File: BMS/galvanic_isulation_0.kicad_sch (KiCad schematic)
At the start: 12 parts

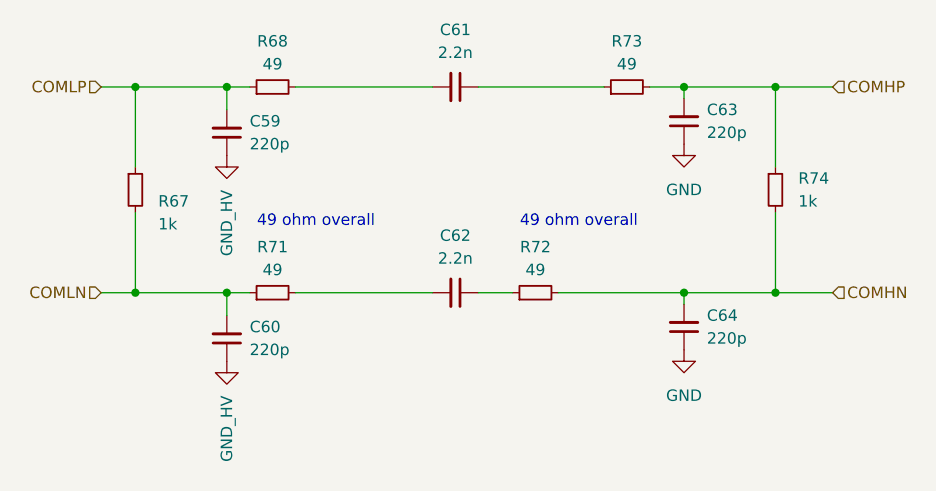
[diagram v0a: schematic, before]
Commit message: Dodano layout drugiego bq79614, ukladu tlumaczącego z protokułu TI na UART oraz wstępnie poprowadzono pary różnicowe
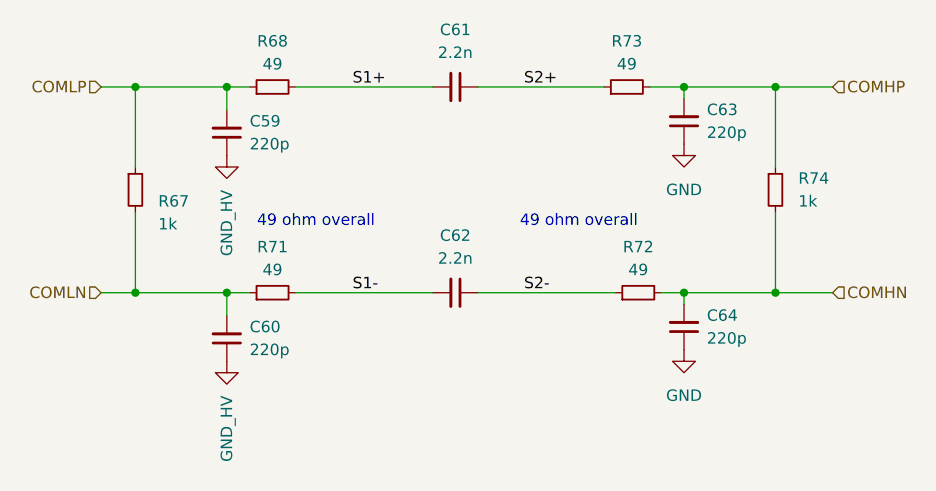
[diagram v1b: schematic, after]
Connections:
- net S1+: now reaches C61.2, R68.2
- net S2+: now reaches C61.1, R73.1
- net S2-: now reaches C62.1, R72.1
- net S1-: now reaches C62.2, R71.2
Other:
- moved on the sheet: R72
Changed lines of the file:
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@@
 	(wire
 		(pts
-			(xy 130.81 97.79) (xy 144.78 97.79)
+			(xy 142.24 97.79) (xy 144.78 97.79)
 		)
 		(stroke
@@
 	(wire
 		(pts
-			(xy 125.73 97.79) (xy 121.92 97.79)
+			(xy 137.16 97.79) (xy 121.92 97.79)
 		)
 		(stroke
@@
 		)
 	)
+	(label "S2+"
+		(at 127 74.93 0)
+		(fields_autoplaced yes)
+		(effects
+			(font
+				(size 1.27 1.27)
+			)
+			(justify left bottom)
+		)
+	)
+	(label "S2-"
+		(at 127 97.79 0)
+		(fields_autoplaced yes)
+		(effects
+			(font
+				(size 1.27 1.27)
+			)
+			(justify left bottom)
+		)
+	)
+	(label "S1-"
+		(at 107.95 97.79 0)
+		(fields_autoplaced yes)
+		(effects
+			(font
+				(size 1.27 1.27)
+			)
+			(justify left bottom)
+		)
+	)
+	(label "S1+"
+		(at 107.95 74.93 0)
+		(fields_autoplaced yes)
+		(effects
+			(font
+				(size 1.27 1.27)
+			)
+			(justify left bottom)
+		)
+	)
 	(hierarchical_label "COMLP"
 		(shape input)
@@
 	(symbol
 		(lib_id "Device:R_Small")
-		(at 128.27 97.79 90)
+		(at 139.7 97.79 90)
 		(unit 1)
 		(exclude_from_sim no)
@@
 		(fields_autoplaced yes)
 		(property "Reference" "R72"
-			(at 128.27 92.71 90)
+			(at 139.7 92.71 90)
 			(effects
 				(font
@@
 		)
 		(property "Value" "49"
-			(at 128.27 95.25 90)
+			(at 139.7 95.25 90)
 			(effects
 				(font
@@
 		)
 		(property "Footprint" "Resistor_SMD:R_0603_1608Metric_Pad0.98x0.95mm_HandSolder"
-			(at 128.27 97.79 0)
+			(at 139.7 97.79 0)
 			(effects
 				(font
@@
 		)
 		(property "Datasheet" "https://www.mouser.pl/ProductDetail/KOA-Speer/RK73H1HRTTCM49R9F?qs=sGAEpiMZZMvdGkrng054txLI%2FDB4oIKDjd1z9Y%252BmyaXFChdzxTCbsQ%3D%3D"
-			(at 128.27 97.79 0)
+			(at 139.7 97.79 0)
 			(effects
 				(font
@@
 		)
 		(property "Description" "Resistor, small symbol"
-			(at 128.27 97.79 0)
-			(effects
-				(font
+			(at 139.7 97.79 0)
+			(effects
+				(font

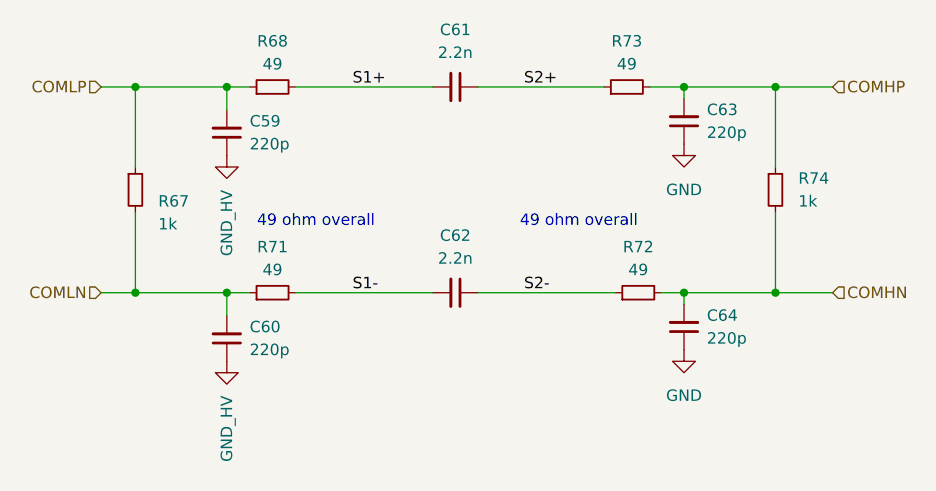
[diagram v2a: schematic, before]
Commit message: Zmienione kondensatory na kondensatory bezpieczeństwa,poprawiono strefy na thermal relief oraz naprawiono bledy z tym zwiazane, impedancja do zmiany jeszcze
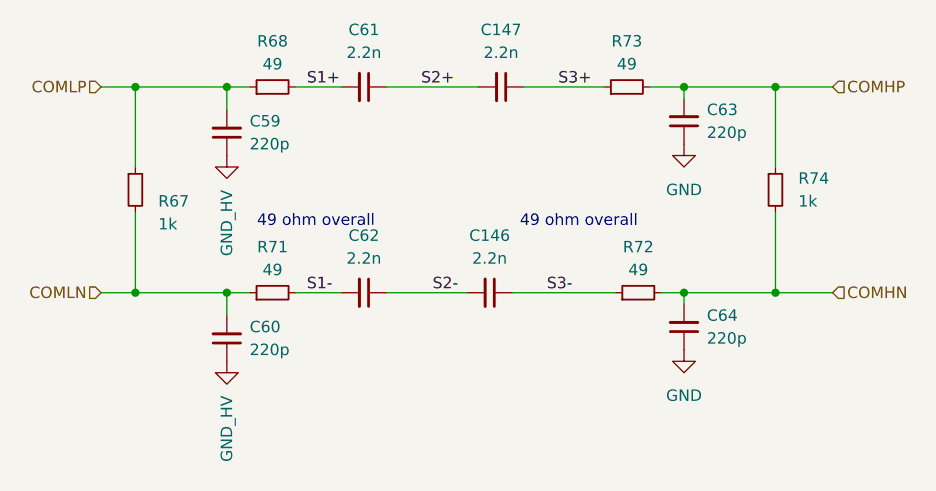
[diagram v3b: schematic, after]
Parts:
- added C146, C147: 2.2n, footrpint:CAPC5728X280N, symbol Device:C_Small
- C61, C62: footprint Capacitor_SMD:C_0603_1608Metric_Pad1.08x0.95mm_HandSolder -> footrpint:CAPC5728X280N
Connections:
- net S2+: now also C147.2; no longer R73.1
- net S2-: now also C146.2; no longer R72.1
- new net S3+: C147.1, R73.1
- new net S3-: C146.1, R72.1
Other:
- moved on the sheet: C61, C62
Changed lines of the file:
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@@
-	(wire
-		(pts
-			(xy 121.92 74.93) (xy 135.89 74.93)
-		)
-		(stroke
-			(width 0)
-			(type default)
-		)
-	)
 	(wire
 		(pts
@@
 	(wire
 		(pts
-			(xy 101.6 97.79) (xy 116.84 97.79)
+			(xy 111.76 97.79) (xy 120.65 97.79)
+		)
+		(stroke
+			(width 0)
+			(type default)
+		)
+	)
+	(wire
+		(pts
+			(xy 101.6 97.79) (xy 106.68 97.79)
 		)
 		(stroke
@@
 	(wire
 		(pts
-			(xy 101.6 74.93) (xy 116.84 74.93)
+			(xy 101.6 74.93) (xy 106.68 74.93)
 		)
 		(stroke
@@
 	(wire
 		(pts
+			(xy 125.73 97.79) (xy 137.16 97.79)
+		)
+		(stroke
+			(width 0)
+			(type default)
+		)
+	)
+	(wire
+		(pts
 			(xy 83.82 88.9) (xy 83.82 97.79)
 		)
@@
 	(wire
 		(pts
+			(xy 111.76 74.93) (xy 121.92 74.93)
+		)
+		(stroke
+			(width 0)
+			(type default)
+		)
+	)
+	(wire
+		(pts
 			(xy 144.78 97.79) (xy 154.94 97.79)
 		)
@@
 	(wire
 		(pts
-			(xy 137.16 97.79) (xy 121.92 97.79)
+			(xy 127 74.93) (xy 135.89 74.93)
 		)
 		(stroke
@@
 	)
 	(label "S2+"
-		(at 127 74.93 0)
+		(at 115.57 74.93 0)
 		(effects
 			(font
@@
 		)
 	)
-	(label "S2-"
-		(at 127 97.79 0)
+	(label "S3+"
+		(at 130.81 74.93 0)
 		(effects
 			(font
@@
 		)
 	)
-	(label "S1-"
-		(at 107.95 97.79 0)
+	(label "S2-"
+		(at 116.84 97.79 0)
 		(effects
 			(font
@@
 		)
 	)
+	(label "S1-"
+		(at 102.87 97.79 0)
+		(effects
+			(font
+				(size 1.27 1.27)
+			)
+			(justify left bottom)
+		)
+	)
+	(label "S3-"
+		(at 129.54 97.79 0)
+		(effects
+			(font
+				(size 1.27 1.27)
+			)
+			(justify left bottom)
+		)
+	)
 	(label "S1+"
-		(at 107.95 74.93 0)
+		(at 102.87 74.93 0)
 		(effects
 			(font
@@
 	(symbol
 		(lib_id "Device:C_Small")
-		(at 119.38 74.93 270)
+		(at 109.22 74.93 270)
 		(unit 1)
 		(exclude_from_sim no)
@@
 		(fields_autoplaced yes)
 		(property "Reference" "C61"
-			(at 119.3736 68.58 90)
+			(at 109.2136 68.58 90)
 			(effects
 				(font
@@
 		)
 		(property "Value" "2.2n"
-			(at 119.3736 71.12 90)
-			(effects
-				(font
-					(size 1.27 1.27)
-				)
-			)
-		)
-		(property "Footprint" "Capacitor_SMD:C_0603_1608Metric_Pad1.08x0.95mm_HandSolder"
-			(at 119.38 74.93 0)
-			(effects
-				(font
-					(size 1.27 1.27)
-				)
-				(hide yes)
-			)
-		)
-		(property "Datasheet" "https://www.mouser.pl/ProductDetail/TDK/CGA3E2C0G1H222J080AE?qs=P1JMDcb91o5KNu2GzASXrQ%3D%3D"
-			(at 119.38 74.93 0)
-			(effects
-				(font
-					(size 1.27 1.27)
-				)
-				(hide yes)
-			)
-		)
-		(property "Description" "Unpolarized capacitor, small symbol"
-			(at 119.38 74.93 0)
+			(at 109.2136 71.12 90)
+			(effects
+				(font
+					(size 1.27 1.27)
+				)
+			)
+		)
+		(property "Footprint" "footrpint:CAPC5728X280N"
+			(at 109.22 74.93 0)
+			(effects
+				(font
+					(size 1.27 1.27)
+				)
+				(hide yes)
+			)
+		)
+		(property "Datasheet" "https://www.mouser.pl/ProductDetail/Walsin/S252B222K502CT?qs=wUXugUrL1qx2Bha0j7hz5g%3D%3D"
+			(at 109.22 74.93 0)
+			(effects
+				(font
+					(size 1.27 1.27)
+				)
+				(hide yes)
+			)
+		)
+		(property "Description" "Kondensator Bezpieczeństwa 250V"
+			(at 109.22 74.93 0)
 			(effects
 				(font
@@
 				(path "/26289bb6-56bc-4ca1-b1a2-18d58d1afdf5/40b62235-494b-489c-87ee-38a07fa46b52"
 					(reference "C61")
+					(unit 1)
+				)
+			)
+		)
+	)
+	(symbol
+		(lib_id "Device:C_Small")
+		(at 123.19 97.79 270)
+		(unit 1)
+		(exclude_from_sim no)
+		(in_bom yes)
+		(on_board yes)
+		(dnp no)
+		(fields_autoplaced yes)
+		(property "Reference" "C146"
+			(at 123.1836 91.44 90)
+			(effects
+				(font
+					(size 1.27 1.27)
+				)
+			)
+		)
+		(property "Value" "2.2n"
+			(at 123.1836 93.98 90)
+			(effects
+				(font
+					(size 1.27 1.27)
+				)
+			)
+		)
+		(property "Footprint" "footrpint:CAPC5728X280N"
+			(at 123.19 97.79 0)
+			(effects
+				(font
+					(size 1.27 1.27)
+				)
+				(hide yes)
+			)
+		)
+		(property "Datasheet" "https://www.mouser.pl/ProductDetail/Walsin/S252B222K502CT?qs=wUXugUrL1qx2Bha0j7hz5g%3D%3D"
+			(at 123.19 97.79 0)
+			(effects
+				(font
+					(size 1.27 1.27)
+				)
+				(hide yes)
+			)
+		)
+		(property "Description" "Kondensator Bezpieczeństwa 250V"
+			(at 123.19 97.79 0)
+			(effects
+				(font
+					(size 1.27 1.27)
+				)
+				(hide yes)
+			)
+		)
+		(pin "2"
+		)
+		(pin "1"
+		)
+		(instances
+			(project "BMS"
+				(path "/26289bb6-56bc-4ca1-b1a2-18d58d1afdf5/40b62235-494b-489c-87ee-38a07fa46b52"
+					(reference "C146")
 					(unit 1)
 				)
@@
 	(symbol
 		(lib_id "Device:C_Small")
-		(at 119.38 97.79 270)
+		(at 109.22 97.79 270)
 		(unit 1)
 		(exclude_from_sim no)
@@
 		(fields_autoplaced yes)
 		(property "Reference" "C62"
-			(at 119.3736 91.44 90)
+			(at 109.2136 91.44 90)
 			(effects
 				(font
@@
 		)
 		(property "Value" "2.2n"
-			(at 119.3736 93.98 90)
-			(effects
-				(font
-					(size 1.27 1.27)
-				)
-			)
-		)
-		(property "Footprint" "Capacitor_SMD:C_0603_1608Metric_Pad1.08x0.95mm_HandSolder"
-			(at 119.38 97.79 0)
-			(effects
-				(font
-					(size 1.27 1.27)
-				)
-				(hide yes)
-			)
-		)
-		(property "Datasheet" "https://www.mouser.pl/ProductDetail/TDK/CGA3E2C0G1H222J080AE?qs=P1JMDcb91o5KNu2GzASXrQ%3D%3D"
-			(at 119.38 97.79 0)
-			(effects
-				(font
-					(size 1.27 1.27)
-				)
-				(hide yes)
-			)
-		)
-		(property "Description" "Unpolarized capacitor, small symbol"
-			(at 119.38 97.79 0)
+			(at 109.2136 93.98 90)
+			(effects
+				(font
+					(size 1.27 1.27)
+				)
+			)
+		)
+		(property "Footprint" "footrpint:CAPC5728X280N"
+			(at 109.22 97.79 0)
+			(effects
+				(font
+					(size 1.27 1.27)
+				)
+				(hide yes)
+			)
+		)
+		(property "Datasheet" "https://www.mouser.pl/ProductDetail/Walsin/S252B222K502CT?qs=wUXugUrL1qx2Bha0j7hz5g%3D%3D"
+			(at 109.22 97.79 0)
+			(effects
+				(font
+					(size 1.27 1.27)
+				)
+				(hide yes)
+			)
+		)
+		(property "Description" "Kondensator Bezpieczeństwa 250V"
+			(at 109.22 97.79 0)
 			(effects
 				(font
@@
 					(unit 1)
 				)
+			)
+		)
+	)
+	(symbol
+		(lib_id "Device:C_Small")
+		(at 124.46 74.93 270)
+		(unit 1)
+		(exclude_from_sim no)
+		(in_bom yes)
+		(on_board yes)
+		(dnp no)
+		(fields_autoplaced yes)
+		(property "Reference" "C147"
+			(at 124.4536 68.58 90)
+			(effects
+				(font
+					(size 1.27 1.27)
+				)
+			)
+		)
+		(property "Value" "2.2n"
+			(at 124.4536 71.12 90)
+			(effects
+				(font
+					(size 1.27 1.27)
+				)
+			)
+		)
+		(property "Footprint" "footrpint:CAPC5728X280N"
+			(at 124.46 74.93 0)
+			(effects
+				(font
+					(size 1.27 1.27)
+				)
+				(hide yes)
+			)
+		)
+		(property "Datasheet" "https://www.mouser.pl/ProductDetail/Walsin/S252B222K502CT?qs=wUXugUrL1qx2Bha0j7hz5g%3D%3D"
+			(at 124.46 74.93 0)
+			(effects
+				(font
+					(size 1.27 1.27)
+				)
+				(hide yes)
+			)
+		)
+		(property "Description" "Kondensator Bezpieczeństwa 250V"
+			(at 124.46 74.93 0)
+			(effects
+				(font
+					(size 1.27 1.27)
+				)
+				(hide yes)
+			)
+		)
+		(pin "2"
+		)
+		(pin "1"
+		)
+		(instances
+			(project "BMS"
+				(path "/26289bb6-56bc-4ca1-b1a2-18d58d1afdf5/40b62235-494b-489c-87ee-38a07fa46b52"
+					(reference "C147")
+					(unit 1)
+				)
